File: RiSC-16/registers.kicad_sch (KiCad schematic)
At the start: 0 parts

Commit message: Continued to flesh out the rom/ram board
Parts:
- added R3, R4: 5K, symbol Device:R_Small_US
- added U10, U12: 28C256, symbol Memory_EEPROM:28C256
- added U11: 74LS139, symbol 74xx:74LS139
- added U13, U14: CY62256-70PC, Package_DIP:DIP-28_W15.24mm, symbol Memory_RAM:CY62256-70PC
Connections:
- new net: R3.2, U10.27 (~{WE})
- new net: R4.2, U12.27 (~{WE})
- new net +5V: R3.1, R4.1, U10.28 (VCC), U11.16 (VCC), U12.28 (VCC), U13.28 (VCC), U14.28 (VCC)
- new net CLK: U11.15 (E)
- new net GND: U10.14 (GND), U11.1 (E), U11.8 (GND), U12.14 (GND), U13.14 (GND), U14.14 (GND)
- new net a0: U10.10 (A0), U12.10 (A0), U13.10 (A0), U14.10 (A0)
- new net a1: U10.9 (A1), U12.9 (A1), U13.9 (A1), U14.9 (A1)
- new net a10: U10.21 (A10), U12.21 (A10), U13.21 (A10), U14.21 (A10)
- new net a11: U10.23 (A11), U12.23 (A11), U13.23 (A11), U14.23 (A11)
- new net a12: U10.2 (A12), U12.2 (A12), U13.2 (A12), U14.2 (A12)
- new net a13: U10.26 (A13), U12.26 (A13), U13.26 (A13), U14.26 (A13)
- new net a14: U10.1 (A14), U11.13 (A1), U11.3 (A1), U12.1 (A14), U13.1 (A14), U14.1 (A14)
- new net a15: U11.14 (A0), U11.2 (A0)
- new net a2: U10.8 (A2), U12.8 (A2), U13.8 (A2), U14.8 (A2)
- new net a3: U10.7 (A3), U12.7 (A3), U13.7 (A3), U14.7 (A3)
- new net a4: U10.6 (A4), U12.6 (A4), U13.6 (A4), U14.6 (A4)
- new net a5: U10.5 (A5), U12.5 (A5), U13.5 (A5), U14.5 (A5)
- new net a6: U10.4 (A6), U12.4 (A6), U13.4 (A6), U14.4 (A6)
- new net a7: U10.3 (A7), U12.3 (A7), U13.3 (A7), U14.3 (A7)
- new net a8: U10.25 (A8), U12.25 (A8), U13.25 (A8), U14.25 (A8)
- new net a9: U10.24 (A9), U12.24 (A9), U13.24 (A9), U14.24 (A9)
- new net d0: U10.11 (D0), U13.11 (Q0), U14.11 (Q0)
- new net d1: U10.12 (D1), U13.12 (Q1), U14.12 (Q1)
- new net d10: U12.13 (D2)
- new net d11: U12.15 (D3)
- new net d12: U12.16 (D4)
- new net d13: U12.17 (D5)
- new net d14: U12.18 (D6)
- new net d15: U12.19 (D7)
- new net d2: U10.13 (D2), U13.13 (Q2), U14.13 (Q2)
- new net d3: U10.15 (D3), U13.15 (Q3), U14.15 (Q3)
- new net d4: U10.16 (D4), U13.16 (Q4), U14.16 (Q4)
- new net d5: U10.17 (D5), U13.17 (Q5), U14.17 (Q5)
- new net d6: U10.18 (D6), U13.18 (Q6), U14.18 (Q6)
- new net d7: U10.19 (D7), U13.19 (Q7), U14.19 (Q7)
- new net d8: U12.11 (D0)
- new net d9: U12.12 (D1)
- new net ~{IO}: U11.7 (O3)
- new net ~{MRD}: U10.22 (~{OE}), U12.22 (~{OE}), U13.22 (~{OE}), U14.22 (~{OE})
- new net ~{MRW}: U13.27 (~{WE}), U14.27 (~{WE})
- new net ~{RAM}: U11.6 (O2), U13.20 (~{CS}), U14.20 (~{CS})
- new net ~{ROM}: U10.20 (~{CS}), U11.4 (O0), U12.20 (~{CS})
- new net ~{SIO}: U11.11 (O1)

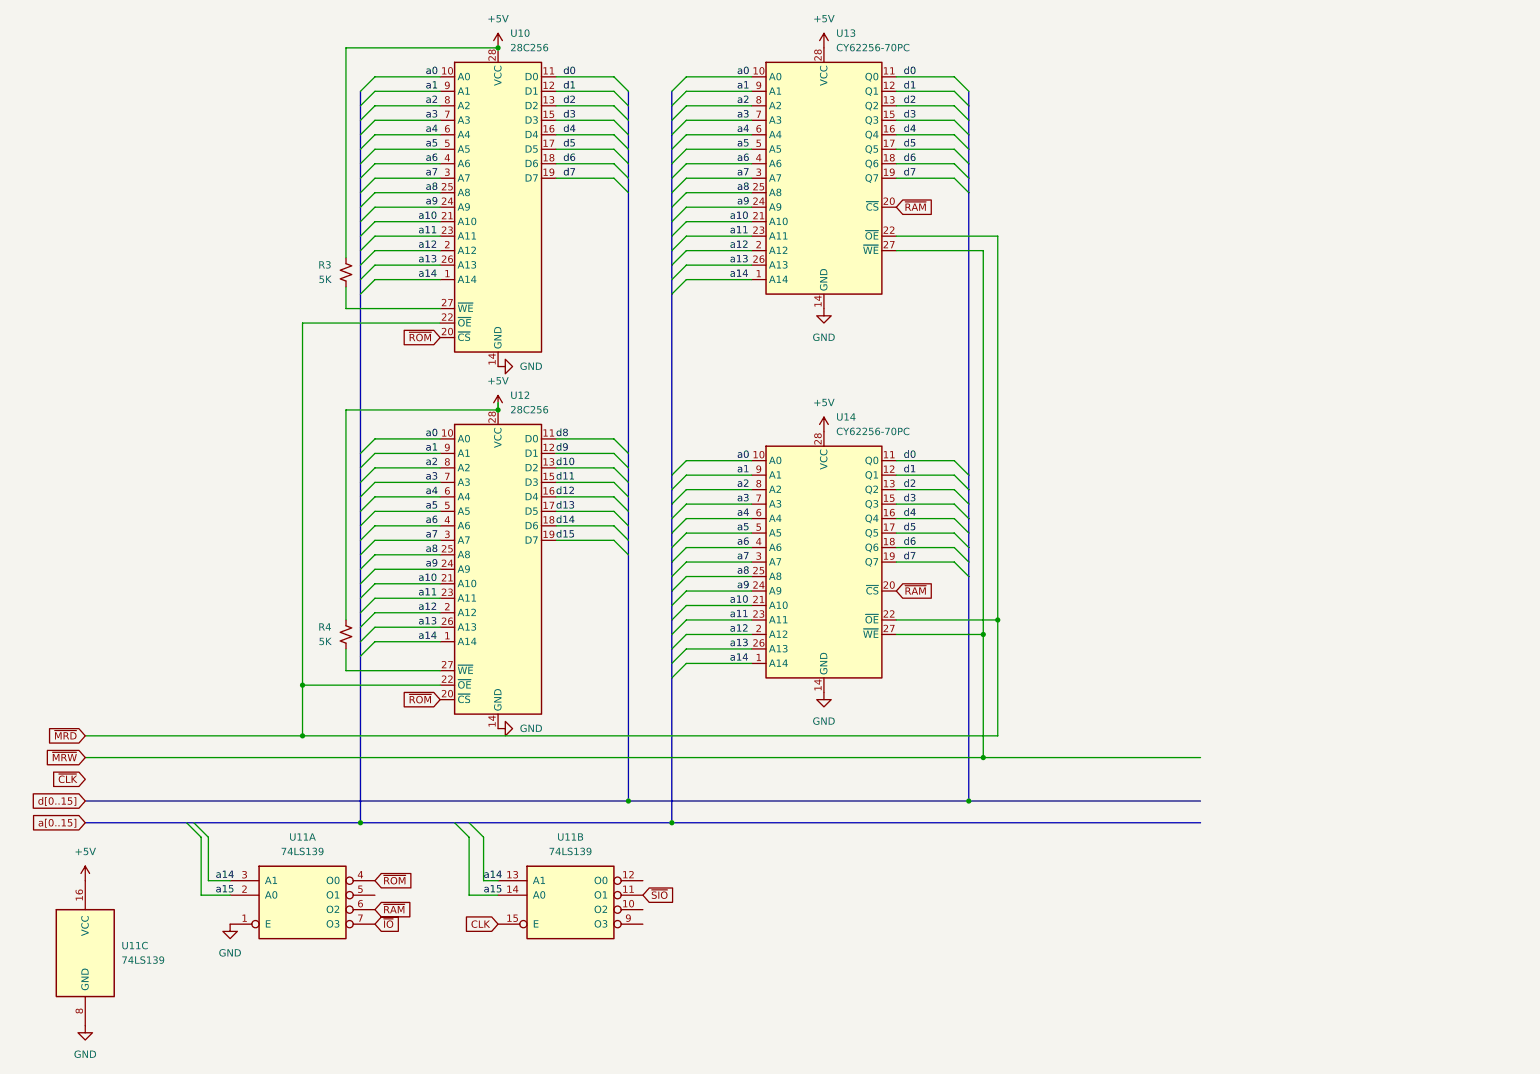
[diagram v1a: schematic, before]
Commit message: Refined instruction register.
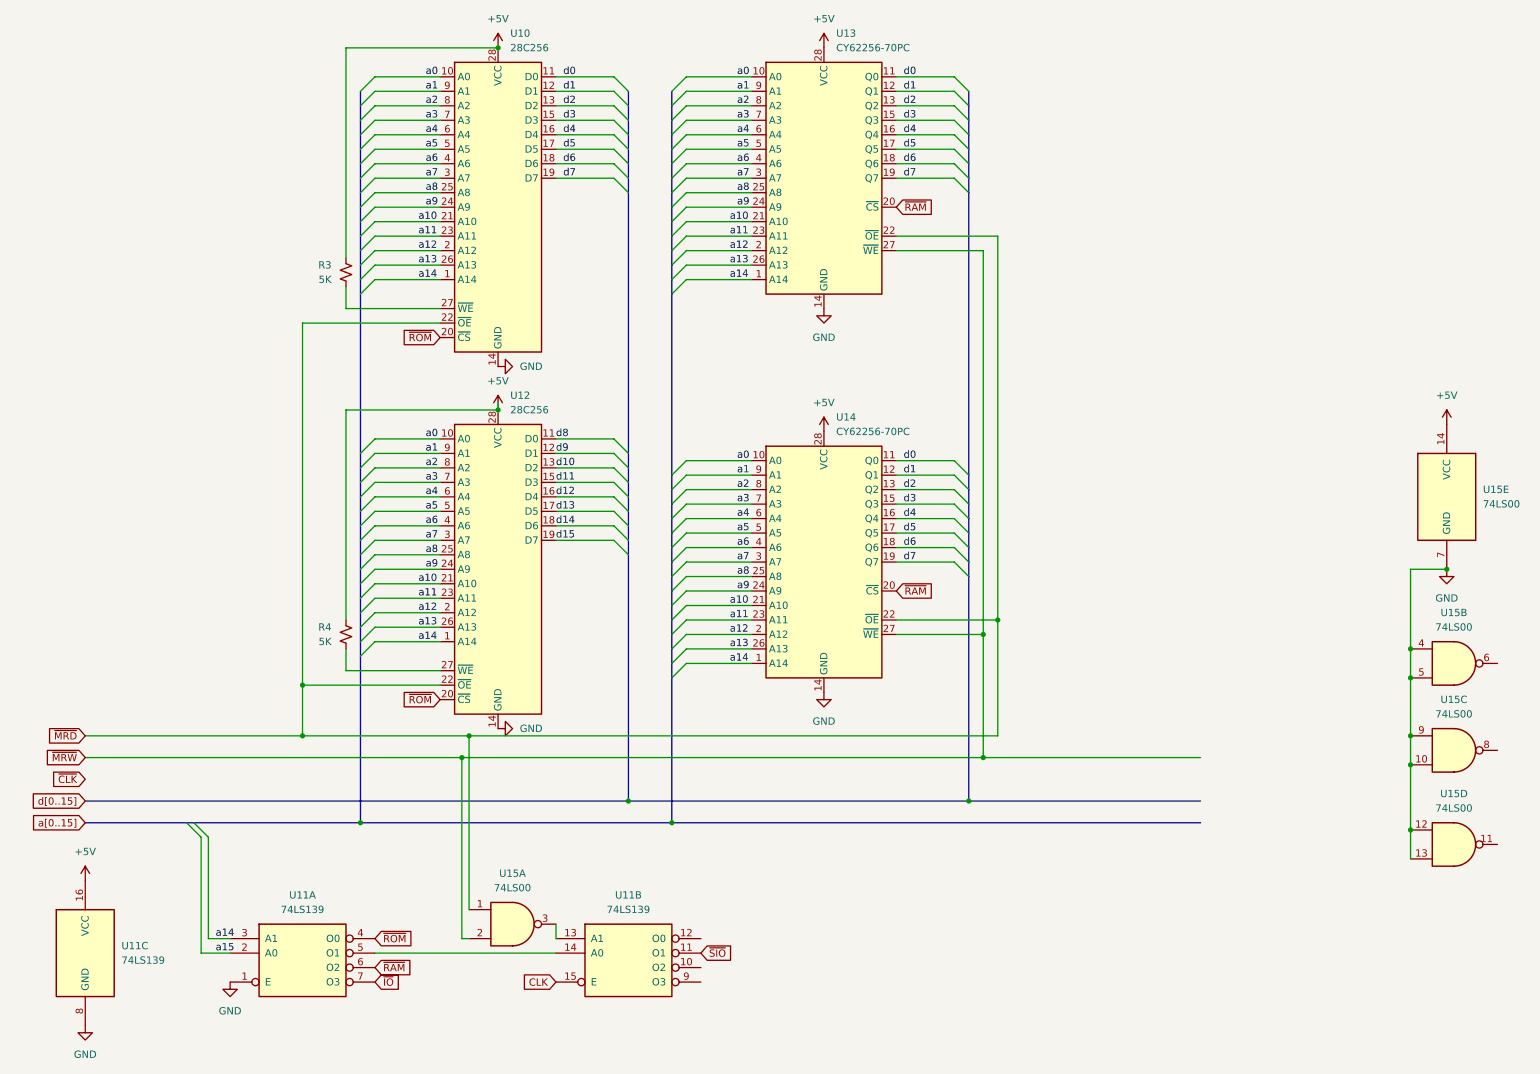
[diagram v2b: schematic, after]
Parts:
- added U15: 74LS00, symbol 74xx:74LS00
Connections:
- net +5V: now also U15.14 (VCC)
- net GND: now also U15.10, U15.12, U15.13, U15.4, U15.5, U15.7 (GND), U15.9
- net a14: no longer U11.13 (A1)
- net a15: no longer U11.14 (A0)
- net ~{MRD}: now also U15.1
- net ~{MRW}: now also U15.2
- net at U11.5 (O1): now also U11.14 (A0)
- new net: U11.13 (A1), U15.3
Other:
- moved on the sheet: U11A, U11B

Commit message: Annotated the schematic to align part numbers. EPROM and RAM board was added last revision. Reworked the src1 latching to assert 0xf to select the PC.
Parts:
- renumbered R3 to R2, R4 to R3, U15 to U11, U14 to U12, U12 to U13, U11 to U14, U13 to U9
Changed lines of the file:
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@@
 		(dnp no)
 		(fields_autoplaced yes)
-		(property "Reference" "#PWR027"
+		(property "Reference" "#PWR030"
 			(at 30.48 168.91 0)
 			(effects
@@
 			(project ""
 				(path "/09ce4153-429f-4803-b069-3af485a81dd6/d0ec361b-fb15-41d2-9c14-09e66b7972d2"
-					(reference "#PWR027")
+					(reference "#PWR030")
 					(unit 1)
 				)
@@
 		(on_board yes)
 		(dnp no)
-		(property "Reference" "R3"
+		(property "Reference" "R2"
 			(at 73.66 57.1499 0)
 			(effects
@@
 			(project ""
 				(path "/09ce4153-429f-4803-b069-3af485a81dd6/d0ec361b-fb15-41d2-9c14-09e66b7972d2"
-					(reference "R3")
+					(reference "R2")
 					(unit 1)
 				)
@@
 		(dnp no)
 		(fields_autoplaced yes)
-		(property "Reference" "U13"
+		(property "Reference" "U9"
 			(at 162.1633 16.51 0)
 			(effects
@@
 			(project ""
 				(path "/09ce4153-429f-4803-b069-3af485a81dd6/d0ec361b-fb15-41d2-9c14-09e66b7972d2"
-					(reference "U13")
+					(reference "U9")
 					(unit 1)
 				)
@@
 		(dnp no)
 		(fields_autoplaced yes)
-		(property "Reference" "U12"
+		(property "Reference" "U13"
 			(at 105.0133 80.01 0)
 			(effects
@@
 			(project "RiSC-16"
 				(path "/09ce4153-429f-4803-b069-3af485a81dd6/d0ec361b-fb15-41d2-9c14-09e66b7972d2"
-					(reference "U12")
+					(reference "U13")
 					(unit 1)
 				)
@@
 		(dnp no)
 		(fields_autoplaced yes)
-		(property "Reference" "#PWR030"
+		(property "Reference" "#PWR029"
 			(at 109.22 138.43 0)
 			(effects
@@
 			(project "RiSC-16"
 				(path "/09ce4153-429f-4803-b069-3af485a81dd6/d0ec361b-fb15-41d2-9c14-09e66b7972d2"
-					(reference "#PWR030")
+					(reference "#PWR029")
 					(unit 1)
 				)
@@
 		(dnp no)
 		(fields_autoplaced yes)
-		(property "Reference" "#PWR036"
+		(property "Reference" "#PWR027"
 			(at 269.24 116.84 0)
 			(effects
@@
 			(project "RiSC-16"
 				(path "/09ce4153-429f-4803-b069-3af485a81dd6/d0ec361b-fb15-41d2-9c14-09e66b7972d2"
-					(reference "#PWR036")
+					(reference "#PWR027")
 					(unit 1)
 				)
@@
 		(dnp no)
 		(fields_autoplaced yes)
-		(property "Reference" "U15"
+		(property "Reference" "U11"
 			(at 270.5017 133.35 0)
 			(effects
@@
 			(project ""
 				(path "/09ce4153-429f-4803-b069-3af485a81dd6/d0ec361b-fb15-41d2-9c14-09e66b7972d2"
-					(reference "U15")
+					(reference "U11")
 					(unit 3)
 				)
@@
 		(dnp no)
 		(fields_autoplaced yes)
-		(property "Reference" "U15"
+		(property "Reference" "U11"
 			(at 105.4017 163.83 0)
 			(effects
@@
 			(project ""
 				(path "/09ce4153-429f-4803-b069-3af485a81dd6/d0ec361b-fb15-41d2-9c14-09e66b7972d2"
-					(reference "U15")
+					(reference "U11")
 					(unit 1)
 				)
@@
 		(dnp no)
 		(fields_autoplaced yes)
-		(property "Reference" "#PWR033"
+		(property "Reference" "#PWR028"
 			(at 160.02 138.43 0)
 			(effects
@@
 			(project "RiSC-16"
 				(path "/09ce4153-429f-4803-b069-3af485a81dd6/d0ec361b-fb15-41d2-9c14-09e66b7972d2"
-					(reference "#PWR033")
+					(reference "#PWR028")
 					(unit 1)
 				)
@@
 		(dnp no)
 		(fields_autoplaced yes)
-		(property "Reference" "U14"
+		(property "Reference" "U12"
 			(at 162.1633 83.82 0)
 			(effects
@@
 			(project ""
 				(path "/09ce4153-429f-4803-b069-3af485a81dd6/d0ec361b-fb15-41d2-9c14-09e66b7972d2"
-					(reference "U14")
+					(reference "U12")
 					(unit 1)
 				)
@@
 		(dnp no)
 		(fields_autoplaced yes)
-		(property "Reference" "#PWR025"
+		(property "Reference" "#PWR031"
 			(at 55.88 189.23 0)
 			(effects
@@
 			(project ""
 				(path "/09ce4153-429f-4803-b069-3af485a81dd6/d0ec361b-fb15-41d2-9c14-09e66b7972d2"
-					(reference "#PWR025")
+					(reference "#PWR031")
 					(unit 1)
 				)
@@
 		(dnp no)
 		(fields_autoplaced yes)
-		(property "Reference" "U15"
+		(property "Reference" "U11"
 			(at 270.5017 118.11 0)
 			(effects
@@
 			(project ""
 				(path "/09ce4153-429f-4803-b069-3af485a81dd6/d0ec361b-fb15-41d2-9c14-09e66b7972d2"
-					(reference "U15")
+					(reference "U11")
 					(unit 2)
 				)
@@
 		(dnp no)
 		(fields_autoplaced yes)
-		(property "Reference" "#PWR026"
+		(property "Reference" "#PWR032"
 			(at 30.48 196.85 0)
 			(effects
@@
 			(project ""
 				(path "/09ce4153-429f-4803-b069-3af485a81dd6/d0ec361b-fb15-41d2-9c14-09e66b7972d2"
-					(reference "#PWR026")
+					(reference "#PWR032")
 					(unit 1)
 				)
@@
 		(dnp no)
 		(fields_autoplaced yes)
-		(property "Reference" "#PWR029"
+		(property "Reference" "#PWR023"
 			(at 109.22 74.93 0)
 			(effects
@@
 			(project "RiSC-16"
 				(path "/09ce4153-429f-4803-b069-3af485a81dd6/d0ec361b-fb15-41d2-9c14-09e66b7972d2"
-					(reference "#PWR029")
+					(reference "#PWR023")
 					(unit 1)
 				)
@@
 		(dnp no)
 		(fields_autoplaced yes)
-		(property "Reference" "U11"
+		(property "Reference" "U14"
 			(at 68.58 167.64 0)
 			(effects
@@
 			(project ""
 				(path "/09ce4153-429f-4803-b069-3af485a81dd6/d0ec361b-fb15-41d2-9c14-09e66b7972d2"
-					(reference "U11")
+					(reference "U14")
 					(unit 1)
 				)
@@
 		(dnp no)
 		(fields_autoplaced yes)
-		(property "Reference" "U11"
+		(property "Reference" "U14"
 			(at 36.83 176.5299 0)
 			(effects
@@
 			(project ""
 				(path "/09ce4153-429f-4803-b069-3af485a81dd6/d0ec361b-fb15-41d2-9c14-09e66b7972d2"
-					(reference "U11")
+					(reference "U14")
 					(unit 3)
 				)
@@
 		(dnp no)
 		(fields_autoplaced yes)
-		(property "Reference" "#PWR031"
+		(property "Reference" "#PWR024"
 			(at 102.87 86.36 0)
 			(effects
@@
 			(project "RiSC-16"
 				(path "/09ce4153-429f-4803-b069-3af485a81dd6/d0ec361b-fb15-41d2-9c14-09e66b7972d2"
-					(reference "#PWR031")
+					(reference "#PWR024")
 					(unit 1)
 				)
@@
 		(dnp no)
 		(fields_autoplaced yes)
-		(property "Reference" "U11"
+		(property "Reference" "U14"
 			(at 125.73 167.64 0)
 			(effects
@@
 			(project ""
 				(path "/09ce4153-429f-4803-b069-3af485a81dd6/d0ec361b-fb15-41d2-9c14-09e66b7972d2"
-					(reference "U11")
+					(reference "U14")
 					(unit 2)
 				)
@@
 		(dnp no)
 		(fields_autoplaced yes)
-		(property "Reference" "#PWR034"
+		(property "Reference" "#PWR026"
 			(at 160.02 90.17 0)
 			(effects
@@
 			(project "RiSC-16"
 				(path "/09ce4153-429f-4803-b069-3af485a81dd6/d0ec361b-fb15-41d2-9c14-09e66b7972d2"
-					(reference "#PWR034")
+					(reference "#PWR026")
 					(unit 1)
 				)
@@
 		(dnp no)
 		(fields_autoplaced yes)
-		(property "Reference" "#PWR035"
+		(property "Reference" "#PWR021"
 			(at 160.02 22.86 0)
 			(effects
@@
 			(project "RiSC-16"
 				(path "/09ce4153-429f-4803-b069-3af485a81dd6/d0ec361b-fb15-41d2-9c14-09e66b7972d2"
-					(reference "#PWR035")
+					(reference "#PWR021")
 					(unit 1)
 				)
@@
 		(dnp no)
 		(fields_autoplaced yes)
-		(property "Reference" "U15"
+		(property "Reference" "U11"
 			(at 275.59 96.5199 0)
 			(effects
@@
 			(project ""
 				(path "/09ce4153-429f-4803-b069-3af485a81dd6/d0ec361b-fb15-41d2-9c14-09e66b7972d2"
-					(reference "U15")
+					(reference "U11")
 					(unit 5)
 				)
@@
 		(dnp no)
 		(fields_autoplaced yes)
-		(property "Reference" "#PWR028"
+		(property "Reference" "#PWR020"
 			(at 102.87 22.86 0)
 			(effects
@@
 			(project "RiSC-16"
 				(path "/09ce4153-429f-4803-b069-3af485a81dd6/d0ec361b-fb15-41d2-9c14-09e66b7972d2"
-					(reference "#PWR028")
+					(reference "#PWR020")
 					(unit 1)
 				)
@@
 		(on_board yes)
 		(dnp no)
-		(property "Reference" "R4"
+		(property "Reference" "R3"
 			(at 73.66 120.6499 0)
 			(effects
@@
 			(project "RiSC-16"
 				(path "/09ce4153-429f-4803-b069-3af485a81dd6/d0ec361b-fb15-41d2-9c14-09e66b7972d2"
-					(reference "R4")
+					(reference "R3")
 					(unit 1)
 				)
@@
 		(dnp no)
 		(fields_autoplaced yes)
-		(property "Reference" "U15"
+		(property "Reference" "U11"
 			(at 270.5017 149.86 0)
 			(effects
@@
 			(project ""
 				(path "/09ce4153-429f-4803-b069-3af485a81dd6/d0ec361b-fb15-41d2-9c14-09e66b7972d2"
-					(reference "U15")
+					(reference "U11")
 					(unit 4)
 				)
@@
 		(dnp no)
 		(fields_autoplaced yes)
-		(property "Reference" "#PWR037"
+		(property "Reference" "#PWR025"
 			(at 269.24 88.9 0)
 			(effects
@@
 			(project "RiSC-16"
 				(path "/09ce4153-429f-4803-b069-3af485a81dd6/d0ec361b-fb15-41d2-9c14-09e66b7972d2"
-					(reference "#PWR037")
+					(reference "#PWR025")
 					(unit 1)
 				)
@@
 		(dnp no)
 		(fields_autoplaced yes)
-		(property "Reference" "#PWR032"
+		(property "Reference" "#PWR022"
 			(at 160.02 71.12 0)
 			(effects
@@
 			(project "RiSC-16"
 				(path "/09ce4153-429f-4803-b069-3af485a81dd6/d0ec361b-fb15-41d2-9c14-09e66b7972d2"
-					(reference "#PWR032")
+					(reference "#PWR022")
 					(unit 1)
 				)
